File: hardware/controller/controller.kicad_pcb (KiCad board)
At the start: 2 copper layers, 150 x 60 mm, 130 parts, among them J1 Conn_01x05, J2 Conn_01x03, J3 Conn_01x04, J4 USB_B_Micro, SW1 ILS_TA180_50, SW10 SW_SPDT, SW2 ILS_TA180_50, SW3 ILS_TA180_50, SW4 ILS_TA180_50, SW5 ILS_TA180_50, SW6 ILS_TA180_50, SW7 ILS_TA180_50, SW8 ILS_TA180_50, SW9 ILS_TA180_50, U1 WS2811, U2 STM32G031F8P6, U3 WS2811, U4 WS2811, U5 HT75xx-1-SOT89, U6 RFM69CW-915MHZ, U7 TP4056

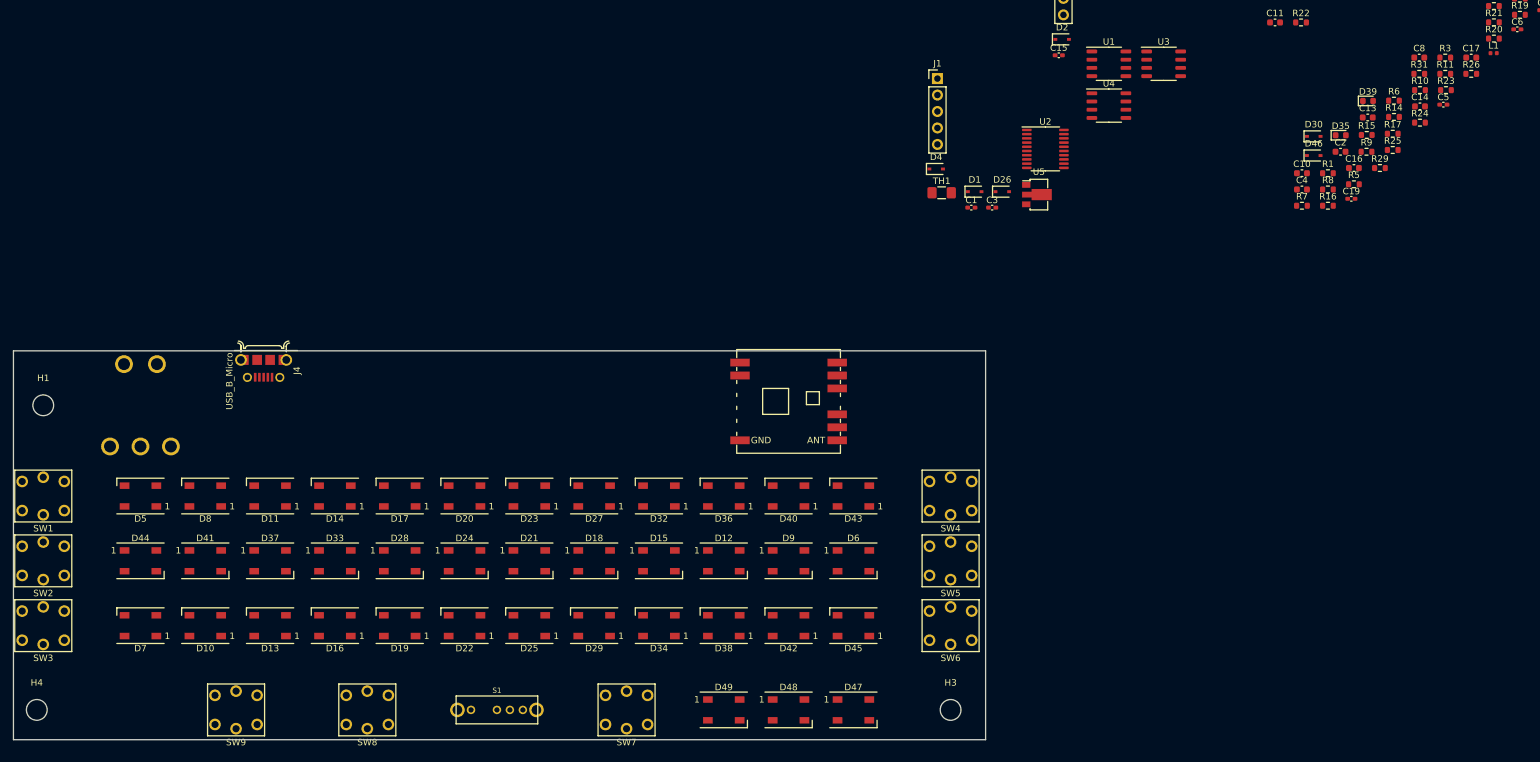
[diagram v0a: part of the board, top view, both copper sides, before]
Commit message: Add controller antenna
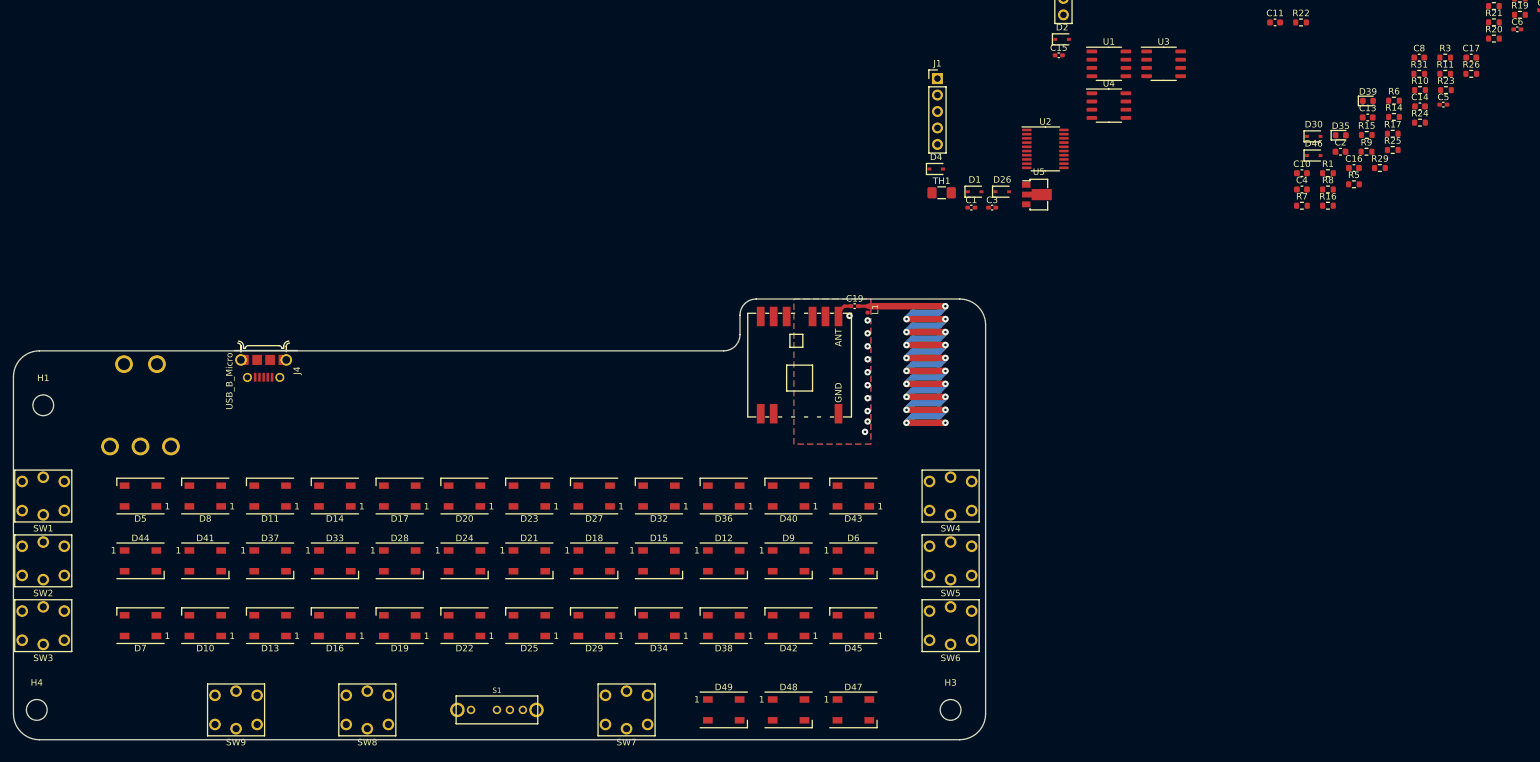
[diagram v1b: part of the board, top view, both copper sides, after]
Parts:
- moved L1 104.4 mm to (162.2, 91.2), turned to 270 degrees
- moved C19 78.4 mm to (160.2, 90.7)
- moved U6 5.85 mm to (151.7, 99.8), turned to 270 degrees
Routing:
- net /ANTENNA: track 0.00 -> 128.9 mm, vias 0 -> 19
- net Net-(C19-Pad1): track 0.00 -> 3.01 mm
- net GND: vias 0 -> 11
- added copper zone on B.Cu, net GND
- added copper zone on F.Cu, net GND
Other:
- board size 150 x 60 mm -> 150 x 68 mm
- rule trace_min: 0.2 -> 0.15

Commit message: Switch to STM32F103
Change-Id: I84217aec2ff83f4d57970417b635599fe3cc7776
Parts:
- added C20: 4.7uF, Capacitor_SMD:C_0603_1608Metric, F.Cu at (174.0, 35.0)
- added C21: 0.1uF, Capacitor_SMD:C_0402_1005Metric_Pad0.74x0.62mm_HandSolder, F.Cu at (173.6, 37.2)
- added C22: 0.1uF, Capacitor_SMD:C_0402_1005Metric_Pad0.74x0.62mm_HandSolder, F.Cu at (177.6, 34.7)
- added C23: 0.1uF, Capacitor_SMD:C_0402_1005Metric_Pad0.74x0.62mm_HandSolder, F.Cu at (173.6, 39.2)
- added C24: 0.1uF, Capacitor_SMD:C_0402_1005Metric_Pad0.74x0.62mm_HandSolder, F.Cu at (176.8, 37.2)
- added JP2: SolderJumper_2_Open, Jumper:SolderJumper-2_P1.3mm_Open_RoundedPad1.0x1.5mm, F.Cu at (174.2, 32.0)
- added R34: 24k, Resistor_SMD:R_0603_1608Metric, F.Cu at (178.3, 31.4)
- U2: value STM32G031F8P6 -> STM32F103C8Tx; footprint Package_SO:TSSOP-20_4.4x6.5mm_P0.65mm -> Package_QFP:LQFP-48_7x7mm_P0.5mm
- moved H2 153.2 mm to (137.5, 102.1)
- moved U2 88.4 mm to (102.8, 82.7)
- moved H1 3.90 mm to (34.9, 102.1)
- moved H3 1.00 mm to (176.0, 153.1)
- moved H4 0.91 mm to (34.9, 153.1)
- moved J4 0.10 mm to (69.0, 99.1)
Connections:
- J4 pad 2: (no net) -> /USB-
- J4 pad 3: (no net) -> /USB+
- U2 pad 1: /LED_OUT -> (no net)
- U2 pad 10: /MISO -> /SW_LEFT
- U2 pad 11: /NSS -> /SW_RIGHT
- U2 pad 12: /DIO0 -> /SW_ACTION
- U2 pad 13: /AUX1 -> /VBATT_DIV
- U2 pad 14: /VBATT_DIV -> /NSS
- U2 pad 15: /SW_LEFT -> /SCK
- U2 pad 16: /SW_RIGHT -> /MISO
- U2 pad 17: /SW_ACTION -> /MOSI
- U2 pad 18: /SWDIO -> /AUX0
- U2 pad 19: /SWCLK -> /AUX1
- U2 pad 4: GND -> (no net)
- U2 pad 5: GND -> (no net)
- U2 pad 6: Net-(C1-Pad2) -> (no net)
- U2 pad 7: /AUX0 -> Net-(C1-Pad2)
- U2 pad 8: /SCK -> GND
- U2 pad 9: /MOSI -> GND

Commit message: Controller layout first pass complete
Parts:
- added C25: 0.1uF, Capacitor_SMD:C_0402_1005Metric_Pad0.74x0.62mm_HandSolder, F.Cu at (79.2, 110.1)
- added D50: D_TVS, Diode_SMD:D_SOD-323, F.Cu at (69.4, 104.8)
- added D51: D_TVS, Diode_SMD:D_SOD-323, F.Cu at (67.3, 104.8)
- C10, C2, C4, C8: value 4.7uF -> 0.1uF; footprint Capacitor_SMD:C_0603_1608Metric -> Capacitor_SMD:C_0402_1005Metric_Pad0.74x0.62mm_HandSolder
- D35: value RED -> GREEN
- J2: moved to B.Cu
- moved R4 251.1 mm to (40.6, 126.9), turned to 90 degrees
- moved R12 247.3 mm to (45.3, 143.0), turned to 270 degrees
- moved R28 232.7 mm to (70.3, 151.6), turned to 90 degrees
- moved C12 223.1 mm to (60.2, 110.5), turned to 90 degrees
- moved C18 223.0 mm to (65.2, 115.2)
- moved R30 222.8 mm to (52.1, 105.8), turned to 180 degrees
- moved R18 219.8 mm to (76.7, 146.5), turned to 270 degrees
- moved R3 219.4 mm to (41.4, 116.1)
- moved R14 215.8 mm to (43.6, 143.0), turned to 270 degrees
- moved R6 215.6 mm to (48.3, 150.8), turned to 270 degrees
- moved R13 213.0 mm to (79.0, 150.8), turned to 270 degrees
- moved C6 212.6 mm to (78.2, 154.0), turned to 90 degrees
- moved R1 208.4 mm to (42.6, 154.4), turned to 270 degrees
- moved R27 207.0 mm to (90.7, 151.6), turned to 270 degrees
- moved R5 207.0 mm to (40.7, 136.9), turned to 270 degrees
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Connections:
- C10 pad 1: /SW_ACTION -> GND
- C10 pad 2: GND -> /SW_MODE
- C14 pad 2: GND -> VCC
- C15 pad 1: GND -> VCC
- C16 pad 2: GND -> VCC
- C20 pad 2: GND -> VCC
- C21 pad 2: GND -> VCC
- C22 pad 1: GND -> VCC
- C23 pad 1: GND -> VCC
- C4 pad 1: GND -> /SW_RIGHT
- C4 pad 2: /SW_MODE -> GND
- C7 pad 2: GND -> VCC
- C8 pad 1: /SW_RIGHT -> /SW_ACTION
- C9 pad 1: GND -> VCC
- D31 pad 1: GND -> VCC
- D47 pad 4: Net-(D45-Pad2) -> Net-(D47-Pad4)
- D49 pad 2: (no net) -> Net-(D49-Pad2)
- D5 pad 4: Net-(D5-Pad4) -> /LED_OUT
- J1 pad 4: GND -> VCC
- J2 pad 1: (no net) -> Net-(J2-Pad1)
- J3 pad 1: GND -> VCC
- J4 pad 4: (no net) -> Net-(J4-Pad4)
- JP2 pad 1: GND -> VCC
- R1 pad 2: /LED_OUT -> Net-(R1-Pad2)
- R11 pad 2: Net-(R11-Pad2) -> Net-(D49-Pad2)
- R15 pad 1: /BLED_3 -> /BLED_5
- R18 pad 1: /BLED_6 -> /BLED_7
- R19 pad 2: GND -> VCC
- R2 pad 2: GND -> VCC
- R22 pad 1: /BLED_5 -> /BLED_3
- R23 pad 1: /BLED_7 -> /BLED_6
- R25 pad 1: Net-(D5-Pad4) -> Net-(D47-Pad4)
- R26 pad 2: GND -> VCC
- R3 pad 2: GND -> VCC
- R7 pad 2: Net-(R7-Pad2) -> Net-(D45-Pad2)
- SW1 pad 2: GND -> Net-(SW1-Pad2)
- SW1 pad 3: (no net) -> Net-(SW1-Pad3)
- SW1 pad 4: (no net) -> GND
- SW10 pad 3: (no net) -> Net-(SW10-Pad3)
- SW2 pad 2: GND -> Net-(SW2-Pad2)
- SW2 pad 3: (no net) -> Net-(SW2-Pad3)
- SW2 pad 4: (no net) -> GND
- SW3 pad 2: GND -> Net-(SW3-Pad2)
- SW3 pad 3: (no net) -> Net-(SW3-Pad3)
- SW3 pad 4: (no net) -> GND
- SW4 pad 2: GND -> Net-(SW4-Pad2)
- SW4 pad 3: (no net) -> Net-(SW4-Pad3)
- SW4 pad 4: (no net) -> GND
- SW5 pad 2: GND -> Net-(SW5-Pad2)
- SW5 pad 3: (no net) -> Net-(SW5-Pad3)
- SW5 pad 4: (no net) -> GND
- SW6 pad 2: GND -> Net-(SW6-Pad2)
- SW6 pad 3: (no net) -> Net-(SW6-Pad3)
- SW6 pad 4: (no net) -> GND
- SW7 pad 2: GND -> Net-(SW7-Pad2)
- SW7 pad 3: (no net) -> Net-(SW7-Pad3)
- SW7 pad 4: (no net) -> GND
- SW8 pad 2: GND -> Net-(SW8-Pad2)
- SW8 pad 3: (no net) -> Net-(SW8-Pad3)
- SW8 pad 4: (no net) -> GND
- SW9 pad 2: GND -> Net-(SW9-Pad2)
- SW9 pad 3: (no net) -> Net-(SW9-Pad3)
- SW9 pad 4: (no net) -> GND
- U1 pad 5: Net-(R7-Pad2) -> Net-(U1-Pad5)
- U1 pad 7: (no net) -> Net-(U1-Pad7)
- U2 pad 1: (no net) -> Net-(U2-Pad1)
- U2 pad 2: (no net) -> Net-(U2-Pad2)
- U2 pad 20: (no net) -> Net-(U2-Pad20)
- U2 pad 21: (no net) -> Net-(U2-Pad21)
- U2 pad 22: (no net) -> Net-(U2-Pad22)
- U2 pad 24: GND -> VCC
- U2 pad 25: (no net) -> Net-(U2-Pad25)
- U2 pad 27: (no net) -> Net-(U2-Pad27)
- U2 pad 29: (no net) -> Net-(U2-Pad29)
- U2 pad 3: (no net) -> Net-(U2-Pad3)
- U2 pad 30: (no net) -> Net-(U2-Pad30)
- U2 pad 31: (no net) -> Net-(U2-Pad31)
- U2 pad 36: GND -> VCC
- U2 pad 38: (no net) -> Net-(U2-Pad38)
- U2 pad 39: (no net) -> Net-(U2-Pad39)
- U2 pad 4: (no net) -> Net-(U2-Pad4)
- U2 pad 40: (no net) -> Net-(U2-Pad40)
- U2 pad 41: (no net) -> Net-(U2-Pad41)
- U2 pad 42: (no net) -> Net-(U2-Pad42)
- U2 pad 43: (no net) -> Net-(U2-Pad43)
- U2 pad 45: (no net) -> Net-(U2-Pad45)
- U2 pad 46: (no net) -> Net-(U2-Pad46)
- U2 pad 48: GND -> VCC
- U2 pad 5: (no net) -> Net-(U2-Pad5)
- U2 pad 6: (no net) -> Net-(U2-Pad6)
- U2 pad 9: GND -> VCC
- U3 pad 5: Net-(R11-Pad2) -> Net-(R25-Pad2)
- U3 pad 7: (no net) -> Net-(U3-Pad7)
- U4 pad 5: Net-(R25-Pad2) -> Net-(R1-Pad2)
- U4 pad 7: (no net) -> Net-(U4-Pad7)
- U5 pad 3: GND -> VCC
- U6 pad 10: (no net) -> Net-(U6-Pad10)
- U6 pad 11: (no net) -> Net-(U6-Pad11)
- U6 pad 12: (no net) -> Net-(U6-Pad12)
- U6 pad 13: (no net) -> Net-(U6-Pad13)
- U6 pad 2: GND -> VCC
- U6 pad 4: (no net) -> Net-(U6-Pad4)
- U7 pad 9: (no net) -> Net-(U7-Pad9)
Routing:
- net VCC: track 0.00 -> 423.5 mm, vias 0 -> 22
- net GND: track 0.00 -> 304.3 mm, vias 11 -> 102
- net /SW_ACTION: track 0.00 -> 93.4 mm, vias 0 -> 4
- net /SW_RIGHT: track 0.00 -> 89.9 mm, vias 0 -> 2
- net /SW_LEFT: track 0.00 -> 83.8 mm, vias 0 -> 2
- net +BATT: track 0.00 -> 80.2 mm, vias 0 -> 3
- net /VBATT_DIV: track 0.00 -> 76.6 mm, vias 0 -> 4
- net /LED_OUT: track 0.00 -> 73.7 mm, vias 0 -> 2
- net Net-(D49-Pad2): track 0.00 -> 62.8 mm
- net /MOSI: track 0.00 -> 57.6 mm, vias 0 -> 2
- net /BLED_6: track 0.00 -> 57.2 mm
- net /NSS: track 0.00 -> 56.8 mm, vias 0 -> 2
- net /SCK: track 0.00 -> 56.1 mm, vias 0 -> 2
- net /DIO0: track 0.00 -> 51.1 mm, vias 0 -> 2
- net /MISO: track 0.00 -> 42.2 mm, vias 0 -> 2
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- added copper zone on F.Cu, net +BATT

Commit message: Controller final hardware v1.0
Change-Id: I90847cb8d53445091bda4f38bed38da399b968f0
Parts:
- added J5: Conn_01x03, Connector_PinHeader_2.54mm:PinHeader_1x03_P2.54mm_Horizontal, B.Cu at (51.6, 146.4)
- added R35: 33R, Resistor_SMD:R_0603_1608Metric, F.Cu at (48.3, 146.2)
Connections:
- J2 pad 1: Net-(J2-Pad1) -> (no net)
- J4 pad 4: Net-(J4-Pad4) -> (no net)
- SW1 pad 2: Net-(SW1-Pad2) -> (no net)
- SW1 pad 3: Net-(SW1-Pad3) -> (no net)
- SW10 pad 3: Net-(SW10-Pad3) -> (no net)
- SW2 pad 2: Net-(SW2-Pad2) -> (no net)
- SW2 pad 3: Net-(SW2-Pad3) -> (no net)
- SW3 pad 2: Net-(SW3-Pad2) -> (no net)
- SW3 pad 3: Net-(SW3-Pad3) -> (no net)
- SW4 pad 2: Net-(SW4-Pad2) -> (no net)
- SW4 pad 3: Net-(SW4-Pad3) -> (no net)
- SW5 pad 2: Net-(SW5-Pad2) -> (no net)
- SW5 pad 3: Net-(SW5-Pad3) -> (no net)
- SW6 pad 2: Net-(SW6-Pad2) -> (no net)
- SW6 pad 3: Net-(SW6-Pad3) -> (no net)
- SW7 pad 2: Net-(SW7-Pad2) -> (no net)
- SW7 pad 3: Net-(SW7-Pad3) -> (no net)
- SW8 pad 2: Net-(SW8-Pad2) -> (no net)
- SW8 pad 3: Net-(SW8-Pad3) -> (no net)
- SW9 pad 2: Net-(SW9-Pad2) -> (no net)
- SW9 pad 3: Net-(SW9-Pad3) -> (no net)
- U1 pad 7: Net-(U1-Pad7) -> (no net)
- U2 pad 1: Net-(U2-Pad1) -> (no net)
- U2 pad 2: Net-(U2-Pad2) -> (no net)
- U2 pad 20: Net-(U2-Pad20) -> (no net)
- U2 pad 21: Net-(U2-Pad21) -> (no net)
- U2 pad 22: Net-(U2-Pad22) -> (no net)
- U2 pad 25: Net-(U2-Pad25) -> (no net)
- U2 pad 27: Net-(U2-Pad27) -> (no net)
- U2 pad 29: Net-(U2-Pad29) -> (no net)
- U2 pad 3: Net-(U2-Pad3) -> (no net)
- U2 pad 30: Net-(U2-Pad30) -> (no net)
- U2 pad 31: Net-(U2-Pad31) -> (no net)
- U2 pad 38: Net-(U2-Pad38) -> (no net)
- U2 pad 39: Net-(U2-Pad39) -> (no net)
- U2 pad 4: Net-(U2-Pad4) -> (no net)
- U2 pad 40: Net-(U2-Pad40) -> (no net)
- U2 pad 41: Net-(U2-Pad41) -> (no net)
- U2 pad 42: Net-(U2-Pad42) -> (no net)
- U2 pad 43: Net-(U2-Pad43) -> (no net)
- U2 pad 45: Net-(U2-Pad45) -> (no net)
- U2 pad 46: Net-(U2-Pad46) -> (no net)
- U2 pad 5: Net-(U2-Pad5) -> (no net)
- U2 pad 6: Net-(U2-Pad6) -> (no net)
- U3 pad 7: Net-(U3-Pad7) -> (no net)
- U4 pad 7: Net-(U4-Pad7) -> (no net)
- U6 pad 10: Net-(U6-Pad10) -> (no net)
- U6 pad 11: Net-(U6-Pad11) -> (no net)
- U6 pad 12: Net-(U6-Pad12) -> (no net)
- U6 pad 13: Net-(U6-Pad13) -> (no net)
- U6 pad 4: Net-(U6-Pad4) -> (no net)
- U7 pad 9: Net-(U7-Pad9) -> (no net)
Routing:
- net Net-(R35-Pad2): track 0.00 -> 10.2 mm, vias 0 -> 2
- net Net-(J5-Pad2): track 0.00 -> 7.51 mm
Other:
- board text added: "+"
- board text added: "-"
- board text added: "3V3"
- board text added: "A0"
- board text added: "A1"
- board text added: "BAT"
- board text added: "BOOT0"
- board text added: "CLK"
- board text added: "G"
- board text added: "GND"
- board text added: "GRN"
- board text added: "IO"
- board text added: "RED"
- board text added: "RST"
- board text added: "firefly-controller v1.0"
- board text added: "off"
- board text added: "on"

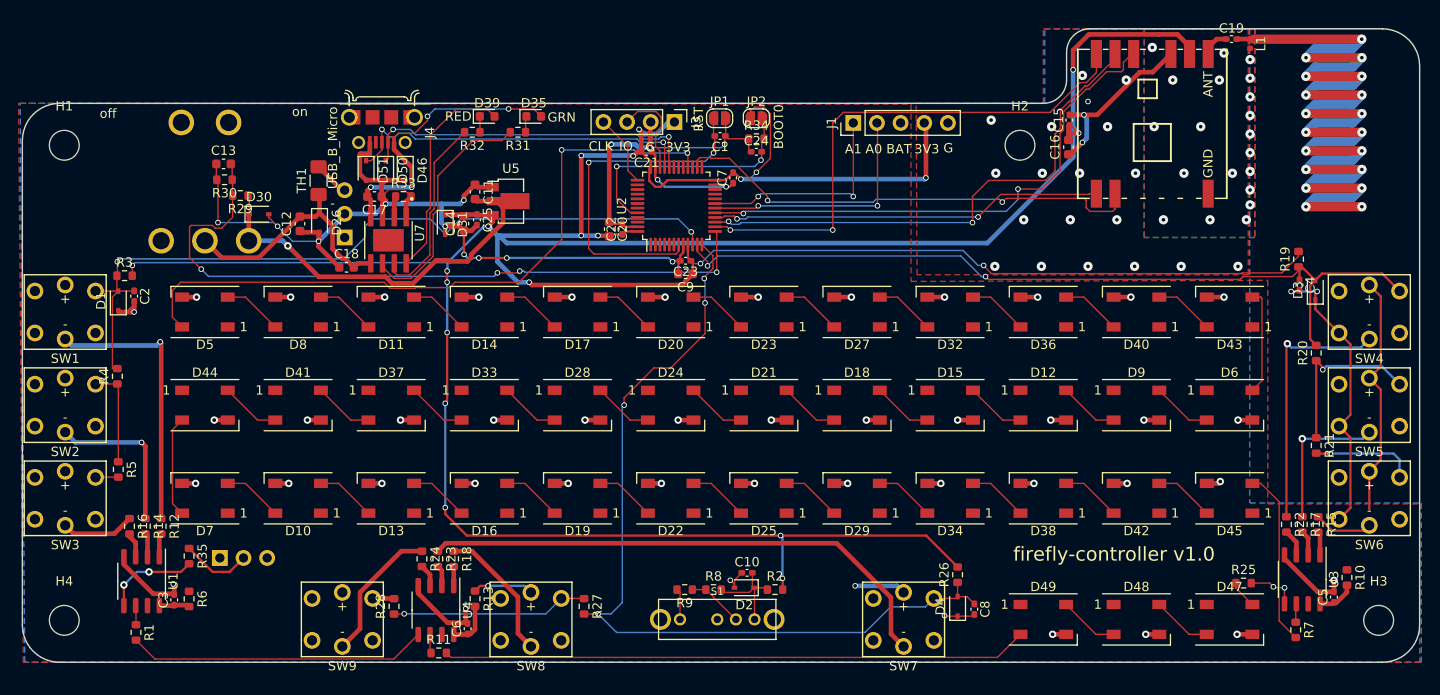
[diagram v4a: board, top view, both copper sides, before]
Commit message: Convert controller to KiCAD v6 and add documentation
Change-Id: I3741fd0f32598f7f607e203966174e99c7ffe945
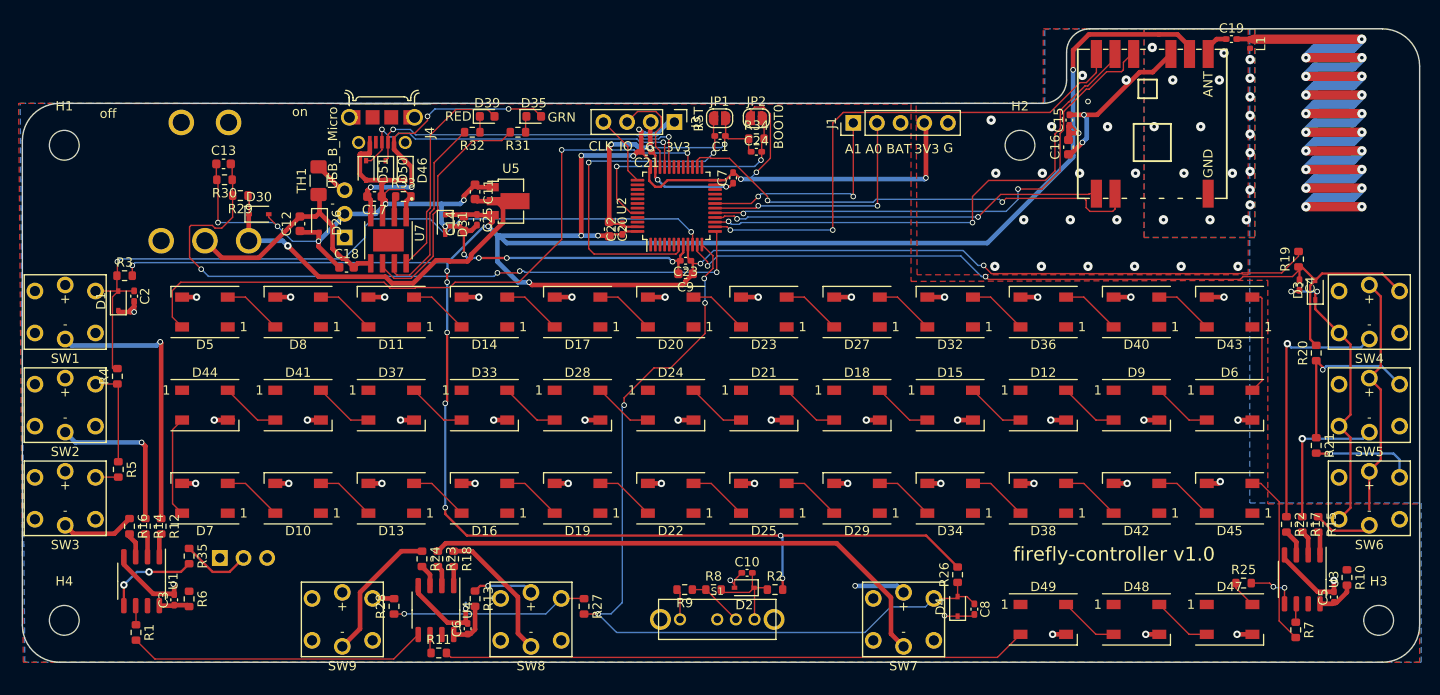
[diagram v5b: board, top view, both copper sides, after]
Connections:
- net /~CHRG renamed /~{CHRG}
- net /~STDBY renamed /~{STDBY}
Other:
- net class Default removed
